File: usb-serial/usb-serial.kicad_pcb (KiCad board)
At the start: 2 copper layers, 39 x 22.5 mm, 17 parts, among them J1 Conn_01x06_Male, Q1 Q_NPN_BCE, Q2 Q_NPN_BCE, U1 C168692, U2 HT7333-A, U3 CH340E

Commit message: usb-c rev-1 rc
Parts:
- added REF**: OSHW-Logo_7.5x8mm_SilkScreen, Symbol:OSHW-Logo_7.5x8mm_SilkScreen, B.Cu at (125.2, 103.8)
- J1: moved to B.Cu
- moved R2 38.3 mm to (125.9, 112.5)
- moved Q1 37.6 mm to (129.7, 111.7), turned to 90 degrees
- moved D2 37.0 mm to (132.6, 109.5), turned to 90 degrees
- moved J1 33.8 mm to (137.0, 109.2)
- moved R3 30.8 mm to (129.6, 108.8), turned to 180 degrees
- moved C4 30.1 mm to (134.5, 105.6), turned to 270 degrees
- moved Q2 29.9 mm to (126.0, 109.5), turned to 270 degrees
- moved C2 27.8 mm to (126.6, 101.6), turned to 90 degrees
- moved R4 25.9 mm to (134.6, 109.5), turned to 270 degrees
- moved C3 24.5 mm to (129.3, 102.5), turned to 180 degrees
- moved U2 21.9 mm to (131.1, 99.0)
- moved U3 21.6 mm to (130.4, 105.5), turned to 270 degrees
- moved R1 18.9 mm to (128.3, 95.3), turned to 180 degrees
- moved C1 18.0 mm to (126.6, 98.2), turned to 90 degrees
- moved D1 13.2 mm to (124.5, 95.3), turned to 180 degrees
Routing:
- net GND: track 28.6 -> 0.00 mm, vias 0 -> 18
- net +3V3: track 0.00 -> 22.7 mm
- net /D-: track 0.00 -> 14.9 mm, vias 0 -> 2
- net /D+: track 0.00 -> 14.8 mm, vias 0 -> 2
- net +5V: track 0.00 -> 13.6 mm
- net /EN: track 0.00 -> 12.5 mm
- net /IO0: track 0.00 -> 11.8 mm
- net /~RTS: track 0.00 -> 8.91 mm
- net /VCC: track 24.2 -> 31.7 mm
- net /~CTS: track 0.00 -> 5.98 mm
- net /RX: track 0.00 -> 5.77 mm
- net /TX: track 0.00 -> 4.77 mm
- net Net-(D2-Pad2): track 0.00 -> 2.08 mm
- net Net-(D2-Pad1): track 0.00 -> 2.01 mm
- net Net-(Q1-Pad1): track 0.00 -> 1.91 mm
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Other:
- board size 39 x 22.5 mm -> 22.1 x 20.5 mm
- board text added: "+3V3"
- board text added: "EN"
- board text added: "GND"
- board text added: "IO0"
- board text added: "REV-1"
- board text added: "RX"
- board text added: "TX"
- board text added: "USB- SERIAL"

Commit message: usb-c rev-1 rc1
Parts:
- removed REF**: OSHW-Logo_7.5x8mm_SilkScreen, Symbol:OSHW-Logo_7.5x8mm_SilkScreen
- J1: footprint Connector_PinHeader_2.00mm:PinHeader_1x06_P2.00mm_Horizontal -> Connector_PinHeader_2.54mm:PinHeader_1x06_P2.54mm_Vertical
- moved J1 0.74 mm to (137.3, 109.8)
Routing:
- net +3V3: track 22.7 -> 24.6 mm
- net /IO0: track 11.8 -> 12.8 mm
- net /RX: track 5.77 -> 6.53 mm
- net /TX: track 4.77 -> 5.30 mm
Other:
- board size 22.1 x 20.5 mm -> 22.6 x 20.5 mm

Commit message: usb-c rev-1 rc1
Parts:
- added REF**: OSHW-Logo_7.5x8mm_SilkScreen, Symbol:OSHW-Logo_7.5x8mm_SilkScreen, B.Cu at (125.3, 103.6)

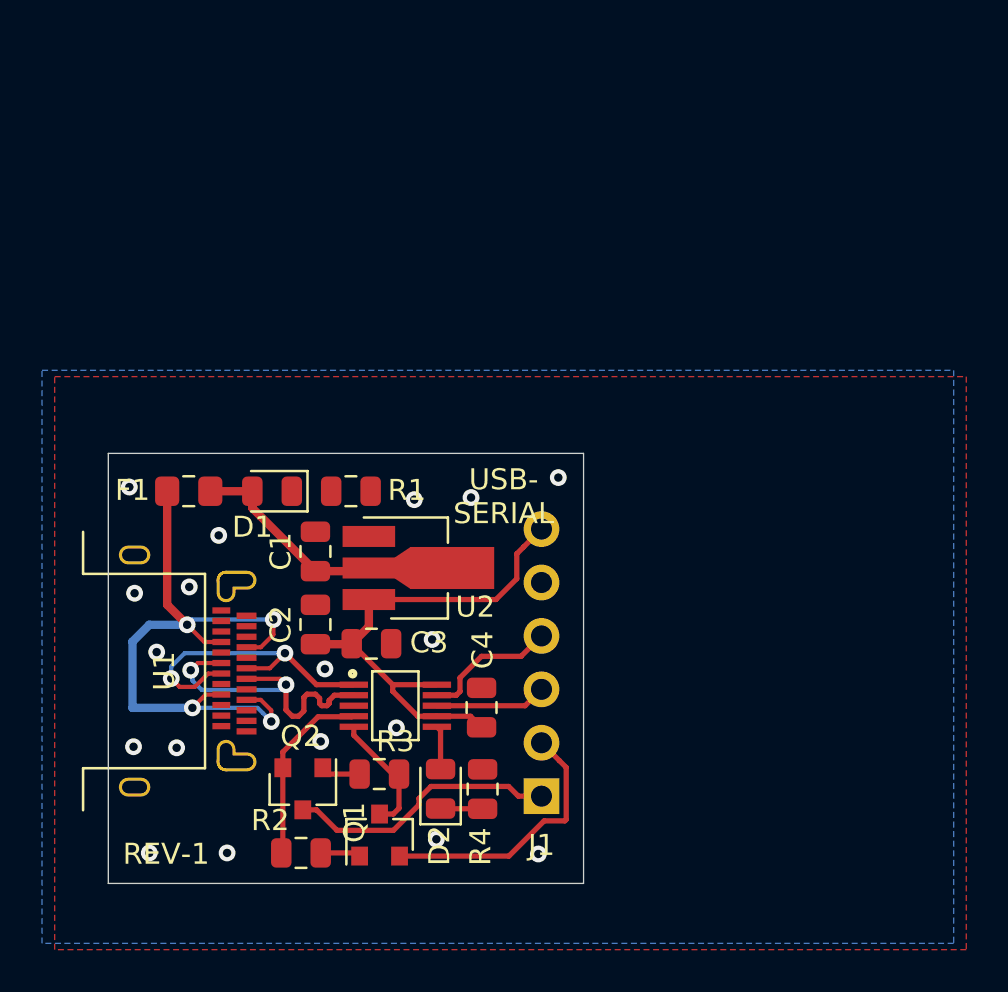
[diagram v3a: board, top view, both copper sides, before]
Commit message: changed usb part
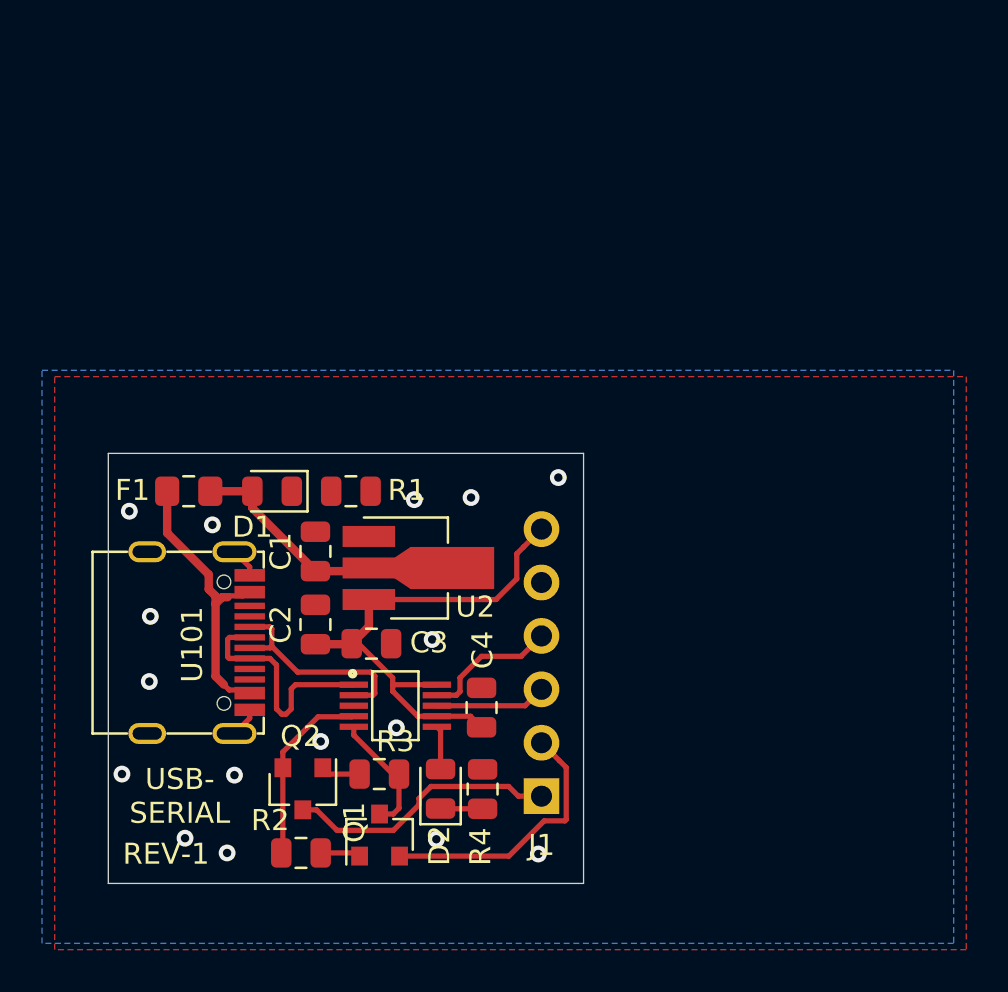
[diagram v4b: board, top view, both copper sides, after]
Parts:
- removed U1: C168692, water-lib:C168692
- added U101: C167321, water-lib:C167321, F.Cu at (122.8, 102.5)
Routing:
- net /VCC: track 31.7 -> 14.2 mm, vias 4 -> 0
- net /D-: track 14.9 -> 10.3 mm, vias 2 -> 0
- net GND: track 0.00 -> 3.44 mm, vias 18 -> 16
- net /D+: track 14.8 -> 11.4 mm, vias 2 -> 0

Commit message: switch RTC <-> CTS
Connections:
- J1 pad 1: /EN -> /IO0
- J1 pad 2: /IO0 -> /EN
- Q1 pad 2: /IO0 -> /EN
- Q2 pad 3: /EN -> /IO0
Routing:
- net Net-(D1-Pad1): track 0.00 -> 1.88 mm
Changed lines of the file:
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@@
-(kicad_pcb (version 20171130) (host pcbnew "(5.1.4-0-10_14)")
+(kicad_pcb (version 20171130) (host pcbnew "(5.1.4)-1")
   (general
     (thickness 1.6)
     (drawings 12)
-    (tracks 132)
+    (tracks 133)
     (zones 0)
     (modules 18)
@@
       (net 14 "Net-(Q1-Pad1)"))
     (pad 2 smd rect (at -1 0.95 90) (size 0.9 0.8) (layers F.Cu F.Paste F.Mask)
-      (net 11 /IO0))
+      (net 10 /EN))
     (pad 3 smd rect (at 1 0 90) (size 0.9 0.8) (layers F.Cu F.Paste F.Mask)
       (net 15 /~CTS))
@@
     )
     (pad 3 smd rect (at 1 0 270) (size 0.9 0.8) (layers F.Cu F.Paste F.Mask)
-      (net 10 /EN))
+      (net 11 /IO0))
     (pad 2 smd rect (at -1 0.95 270) (size 0.9 0.8) (layers F.Cu F.Paste F.Mask)
       (net 16 /~RTS))
@@
     )
     (pad 1 thru_hole rect (at 0 0) (size 1.7 1.7) (drill 1) (layers *.Cu *.Mask)
+      (net 11 /IO0))
+    (pad 2 thru_hole oval (at 0 -2.54) (size 1.7 1.7) (drill 1) (layers *.Cu *.Mask)
       (net 10 /EN))
-    (pad 2 thru_hole oval (at 0 -2.54) (size 1.7 1.7) (drill 1) (layers *.Cu *.Mask)
-      (net 11 /IO0))
     (pad 3 thru_hole oval (at 0 -5.08) (size 1.7 1.7) (drill 1) (layers *.Cu *.Mask)
       (net 12 /TX))
@@
     (effects (font (size 1 1) (thickness 0.15)) (justify mirror))
   )
-  (gr_text IO0 (at 134.4 107.4) (layer B.SilkS)
+  (gr_text IO0 (at 134.4 109.95) (layer B.SilkS)
     (effects (font (size 1 1) (thickness 0.15)) (justify mirror))
   )
-  (gr_text EN (at 134.65 109.95) (layer B.SilkS)
+  (gr_text EN (at 134.6 107.2) (layer B.SilkS)
     (effects (font (size 1 1) (thickness 0.15)) (justify mirror))
   )
@@
   (segment (start 123.475 103.25) (end 124.435002 103.25) (width 0.25) (layer F.Cu) (net 4))
   (segment (start 122.5 103.25) (end 123.475 103.25) (width 0.25) (layer F.Cu) (net 4))
+  (segment (start 123.475 102.25) (end 122.514998 102.25) (width 0.25) (layer F.Cu) (net 4))
+  (segment (start 122.424999 102.339999) (end 122.424999 103.174999) (width 0.25) (layer F.Cu) (net 4))
+  (segment (start 122.424999 103.174999) (end 122.5 103.25) (width 0.25) (layer F.Cu) (net 4))
   (segment (start 122.514998 102.25) (end 122.424999 102.339999) (width 0.25) (layer F.Cu) (net 4))
-  (segment (start 122.424999 103.174999) (end 122.5 103.25) (width 0.25) (layer F.Cu) (net 4))
-  (segment (start 122.424999 102.339999) (end 122.424999 103.174999) (width 0.25) (layer F.Cu) (net 4))
-  (segment (start 123.475 102.25) (end 122.514998 102.25) (width 0.25) (layer F.Cu) (net 4))
   (segment (start 129.425001 104.910001) (end 129.425001 104.089999) (width 0.25) (layer F.Cu) (net 5))
   (segment (start 128.425 105) (end 129.335002 105) (width 0.25) (layer F.Cu) (net 5))
@@
   (segment (start 131.464998 106) (end 130.275 104.810002) (width 0.25) (layer F.Cu) (net 6))
   (segment (start 132.375 106) (end 131.464998 106) (width 0.25) (layer F.Cu) (net 6))
+  (segment (start 125.475 95.3) (end 127.35 95.3) (width 0.25) (layer F.Cu) (net 7))
   (segment (start 132.55 106.675) (end 132.375 106.5) (width 0.25) (layer F.Cu) (net 8))
   (segment (start 132.55 108.5125) (end 132.55 106.675) (width 0.25) (layer F.Cu) (net 8))
   (segment (start 132.5625 110.4) (end 132.55 110.3875) (width 0.25) (layer F.Cu) (net 9))
   (segment (start 134.55 110.4) (end 132.5625 110.4) (width 0.25) (layer F.Cu) (net 9))
-  (segment (start 131.52499 109.90816) (end 132.09564 109.33751) (width 0.25) (layer F.Cu) (net 10))
-  (segment (start 131.52499 110.210012) (end 131.52499 109.90816) (width 0.25) (layer F.Cu) (net 10))
-  (segment (start 130.310001 111.425001) (end 131.52499 110.210012) (width 0.25) (layer F.Cu) (net 10))
-  (segment (start 127.625001 111.425001) (end 130.310001 111.425001) (width 0.25) (layer F.Cu) (net 10))
-  (segment (start 126.65 110.45) (end 127.625001 111.425001) (width 0.25) (layer F.Cu) (net 10))
-  (segment (start 126 110.45) (end 126.65 110.45) (width 0.25) (layer F.Cu) (net 10))
-  (segment (start 136.25 109.8) (end 137.35 109.8) (width 0.25) (layer F.Cu) (net 10))
-  (segment (start 135.78751 109.33751) (end 136.25 109.8) (width 0.25) (layer F.Cu) (net 10))
-  (segment (start 132.09564 109.33751) (end 135.78751 109.33751) (width 0.25) (layer F.Cu) (net 10))
-  (segment (start 138.199999 108.109999) (end 137.35 107.26) (width 0.25) (layer F.Cu) (net 11))
-  (segment (start 138.525001 108.435001) (end 138.199999 108.109999) (width 0.25) (layer F.Cu) (net 11))
-  (segment (start 138.525001 110.910001) (end 138.525001 108.435001) (width 0.25) (layer F.Cu) (net 11))
-  (segment (start 138.460001 110.975001) (end 138.525001 110.910001) (width 0.25) (layer F.Cu) (net 11))
-  (segment (start 137.474999 110.975001) (end 138.460001 110.975001) (width 0.25) (layer F.Cu) (net 11))
-  (segment (start 135.8 112.65) (end 137.474999 110.975001) (width 0.25) (layer F.Cu) (net 11))
-  (segment (start 130.6 112.65) (end 135.8 112.65) (width 0.25) (layer F.Cu) (net 11))
+  (segment (start 131.52499 109.90816) (end 132.09564 109.33751) (width 0.25) (layer F.Cu) (net 11))
+  (segment (start 131.52499 110.210012) (end 131.52499 109.90816) (width 0.25) (layer F.Cu) (net 11))
+  (segment (start 130.310001 111.425001) (end 131.52499 110.210012) (width 0.25) (layer F.Cu) (net 11))
+  (segment (start 127.625001 111.425001) (end 130.310001 111.425001) (width 0.25) (layer F.Cu) (net 11))
+  (segment (start 126.65 110.45) (end 127.625001 111.425001) (width 0.25) (layer F.Cu) (net 11))
+  (segment (start 126 110.45) (end 126.65 110.45) (width 0.25) (layer F.Cu) (net 11))
+  (segment (start 136.25 109.8) (end 137.35 109.8) (width 0.25) (layer F.Cu) (net 11))
+  (segment (start 135.78751 109.33751) (end 136.25 109.8) (width 0.25) (layer F.Cu) (net 11))
+  (segment (start 132.09564 109.33751) (end 135.78751 109.33751) (width 0.25) (layer F.Cu) (net 11))
+  (segment (start 138.199999 108.109999) (end 137.35 107.26) (width 0.25) (layer F.Cu) (net 10))
+  (segment (start 138.525001 108.435001) (end 138.199999 108.109999) (width 0.25) (layer F.Cu) (net 10))
+  (segment (start 138.525001 110.910001) (end 138.525001 108.435001) (width 0.25) (layer F.Cu) (net 10))
+  (segment (start 138.460001 110.975001) (end 138.525001 110.910001) (width 0.25) (layer F.Cu) (net 10))
+  (segment (start 137.474999 110.975001) (end 138.460001 110.975001) (width 0.25) (layer F.Cu) (net 10))
+  (segment (start 135.8 112.65) (end 137.474999 110.975001) (width 0.25) (layer F.Cu) (net 10))
+  (segment (start 130.6 112.65) (end 135.8 112.65) (width 0.25) (layer F.Cu) (net 10))
   (segment (start 136.57 105.5) (end 137.35 104.72) (width 0.25) (layer F.Cu) (net 12))
   (segment (start 132.375 105.5) (end 136.57 105.5) (width 0.25) (layer F.Cu) (net 12))
